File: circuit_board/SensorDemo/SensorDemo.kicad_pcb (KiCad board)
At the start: 2 copper layers, 14 parts, among them J1 BARREL_JACK, SW1 SWITCH_SPDT, U1 TLV1117-33CDCYR, U2 MCP4821, U3 dsPIC33EP32GP502

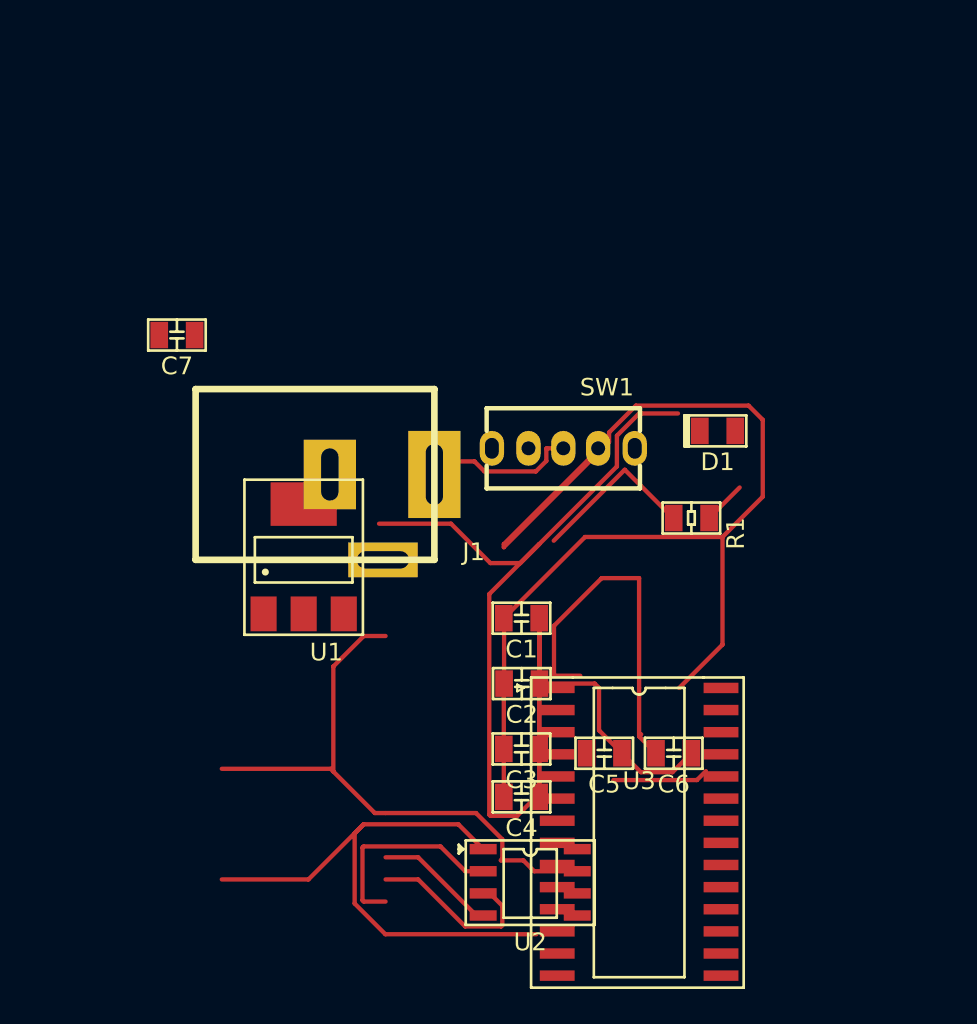
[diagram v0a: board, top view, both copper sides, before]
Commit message: updated schematic
added footprints to everything and minor changes to 6pin
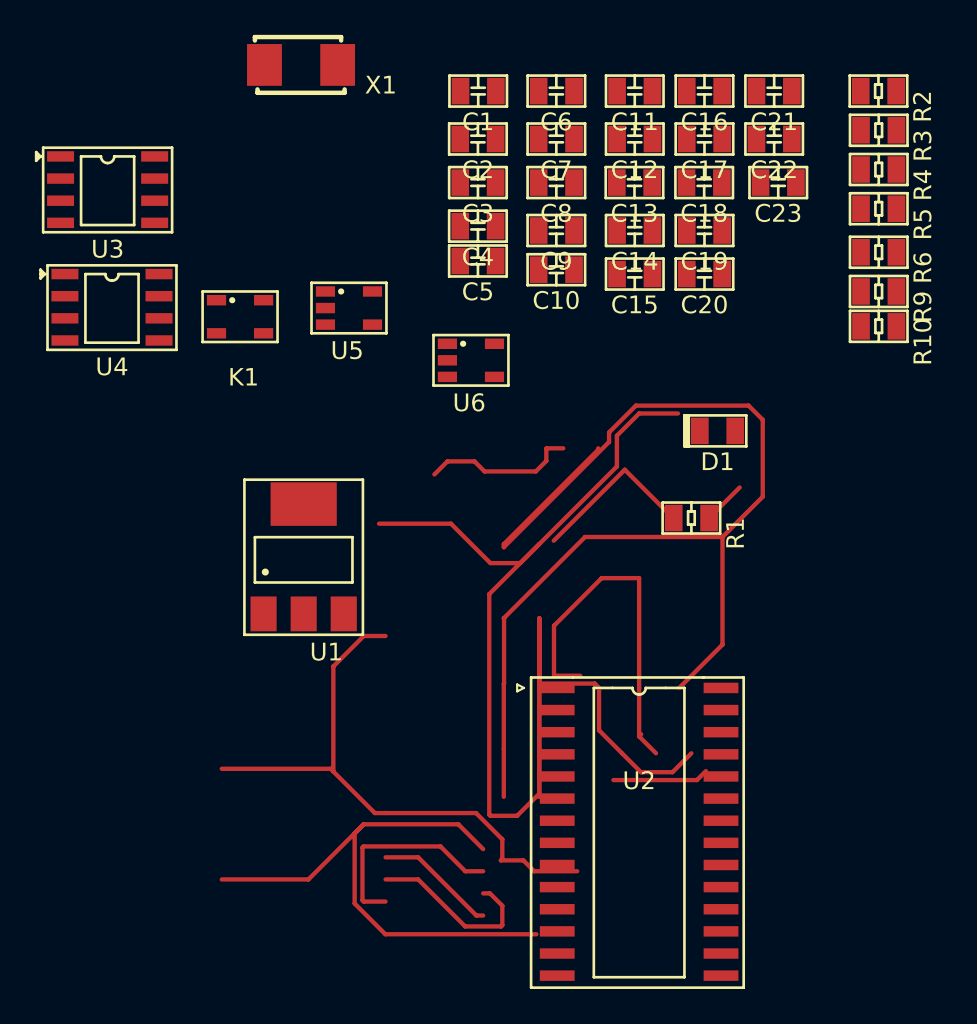
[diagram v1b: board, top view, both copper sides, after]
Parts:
- removed J1: BARREL_JACK, Global PCB Library:BARREL_JACK
- removed SW1: SWITCH_SPDT, SensorDemo_pcb:SW_OS102011MA1QN1
- removed the U2 at (88.0, 80.5)
- added C10: 0.1uF, SensorDemo_pcb:C0805, F.Cu at (89.5, 47.2)
- added C11: 0.1uF, SensorDemo_pcb:C0805, F.Cu at (94.0, 37.0)
- added C12: 1uF, SensorDemo_pcb:C0805, F.Cu at (94.0, 39.8)
- added C13: .1uF, SensorDemo_pcb:C0805, F.Cu at (94.0, 42.2)
- added C14: 0.1uF, SensorDemo_pcb:C0805, F.Cu at (94.0, 45.0)
- added C15: 1uF, SensorDemo_pcb:C0805, F.Cu at (94.0, 47.5)
- added C16: 0.1uF, SensorDemo_pcb:C0805, F.Cu at (98.0, 37.0)
- added C17: 1uF, SensorDemo_pcb:C0805, F.Cu at (98.0, 39.8)
- added C18: .1uF, SensorDemo_pcb:C0805, F.Cu at (98.0, 42.2)
- added C19: 0.1uF, SensorDemo_pcb:C0805, F.Cu at (98.0, 45.0)
- added C20: 1uF, SensorDemo_pcb:C0805, F.Cu at (98.0, 47.5)
- added C21: 1uF, SensorDemo_pcb:C0805, F.Cu at (102.0, 37.0)
- added C22: .1uF, SensorDemo_pcb:C0805, F.Cu at (102.0, 39.8)
- added C23: .1uF, SensorDemo_pcb:C0805, F.Cu at (102.2, 42.2)
- added C8: 0.1uF, SensorDemo_pcb:C0805, F.Cu at (89.5, 42.2)
- added C9: 1uF, SensorDemo_pcb:C0805, F.Cu at (89.5, 45.0)
- added K1: PB, SensorDemo_pcb:SOT-23-4, F.Cu at (70.0, 49.0)
- added R10: 0, SensorDemo_pcb:R0805, F.Cu at (108.0, 50.5)
- added R2: R, SensorDemo_pcb:R0805, F.Cu at (108.0, 37.0)
- added R3: 10k, SensorDemo_pcb:R0805, F.Cu at (108.0, 39.2)
- added R4: R, SensorDemo_pcb:R0805, F.Cu at (108.0, 41.5)
- added R5: 0, SensorDemo_pcb:R0805, F.Cu at (108.0, 43.8)
- added R6: 100R, SensorDemo_pcb:R0805, F.Cu at (108.0, 46.2)
- added R9: 100R, SensorDemo_pcb:R0805, F.Cu at (108.0, 48.5)
- added U3: LTC1658, SensorDemo_pcb:SOIC-8, F.Cu at (63.8, 40.8)
- added U4: INA126, SensorDemo_pcb:SOIC-8, F.Cu at (64.0, 47.5)
- added U5: REF1925, SensorDemo_pcb:SOT-23-5, F.Cu at (76.2, 48.5)
- added U6: REF1925, SensorDemo_pcb:SOT-23-5, F.Cu at (83.2, 51.5)
- added X1: CRYSTAL, SensorDemo_pcb:CRYSTAL_ABM3-8.000MHz-D2Y-T, F.Cu at (74.8, 35.5)
- C1: value 10uF -> C
- C2: value 1uF -> .01uF
- C3: value 1uF -> C
- C4: value 100nF -> 0.1uF
- C5: value 100nF -> 10nF
- C6: value 1uF -> 10uF
- C7: value 100nF -> 1uF
- R1: value 330R -> 1k
- moved C6 38.6 mm to (89.5, 37.0)
- moved C4 32.8 mm to (85.0, 44.8)
- moved C3 32.6 mm to (85.0, 42.2)
- moved C2 31.4 mm to (85.0, 39.8)
- moved C1 30.4 mm to (85.0, 37.0)
- moved C5 29.2 mm to (85.0, 46.8)
- moved C7 24.5 mm to (89.5, 39.8)
- renumbered U3 to U2
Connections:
- C1 pad 2: Net-(C1-Pad2) -> GND
- C2 pad 1: Net-(C1-Pad1) -> Net-(C2-Pad1)
- C2 pad 2: Net-(C1-Pad2) -> GND
- C3 pad 1: Net-(C1-Pad1) -> Net-(C3-Pad1)
- C3 pad 2: Net-(C1-Pad2) -> GND
- C4 pad 1: Net-(C1-Pad1) -> /Vref
- C4 pad 2: Net-(C1-Pad2) -> GND
- C5 pad 1: Net-(C1-Pad1) -> Net-(C10-Pad1)
- C5 pad 2: Net-(C1-Pad2) -> GND
- C6 pad 1: +3V3 -> Net-(C10-Pad1)
- C6 pad 2: Net-(C1-Pad2) -> GND
- C7 pad 1: +3V3 -> Net-(C10-Pad1)
- C7 pad 2: Net-(C1-Pad2) -> GND
- D1 pad 2: Net-(C1-Pad2) -> GND
- U1 pad 1: Net-(C1-Pad2) -> GND
- U1 pad 3: Net-(C1-Pad1) -> Net-(C10-Pad1)
- U2 pad 1: (no net) -> Net-(C2-Pad1)
- U2 pad 10: (no net) -> Net-(U2-Pad10)
- U2 pad 11: (no net) -> Net-(U2-Pad11)
- U2 pad 12: (no net) -> Net-(U2-Pad12)
- U2 pad 14: (no net) -> Net-(U2-Pad14)
- U2 pad 15: /~CS -> Net-(U2-Pad15)
- U2 pad 16: /SCK -> Net-(U2-Pad16)
- U2 pad 17: /SDI -> Net-(U2-Pad17)
- U2 pad 18: (no net) -> Net-(U2-Pad18)
- U2 pad 2: (no net) -> /sensVal
- U2 pad 20: (no net) -> Net-(TC1-Pad1)
- U2 pad 21: (no net) -> /ucTX
- U2 pad 22: (no net) -> /ucRX
- U2 pad 23: (no net) -> Net-(U2-Pad23)
- U2 pad 24: (no net) -> Net-(U2-Pad24)
- U2 pad 25: (no net) -> Net-(U2-Pad25)
- U2 pad 26: (no net) -> Net-(U2-Pad26)
- U2 pad 28: (no net) -> Net-(C8-Pad1)
- U2 pad 3: (no net) -> Net-(U2-Pad3)
- U2 pad 4: (no net) -> GND
- U2 pad 5: (no net) -> /Vref
- U2 pad 6: (no net) -> /PGC
- U2 pad 7: (no net) -> /PGD
- U2 pad 9: (no net) -> Net-(U2-Pad9)

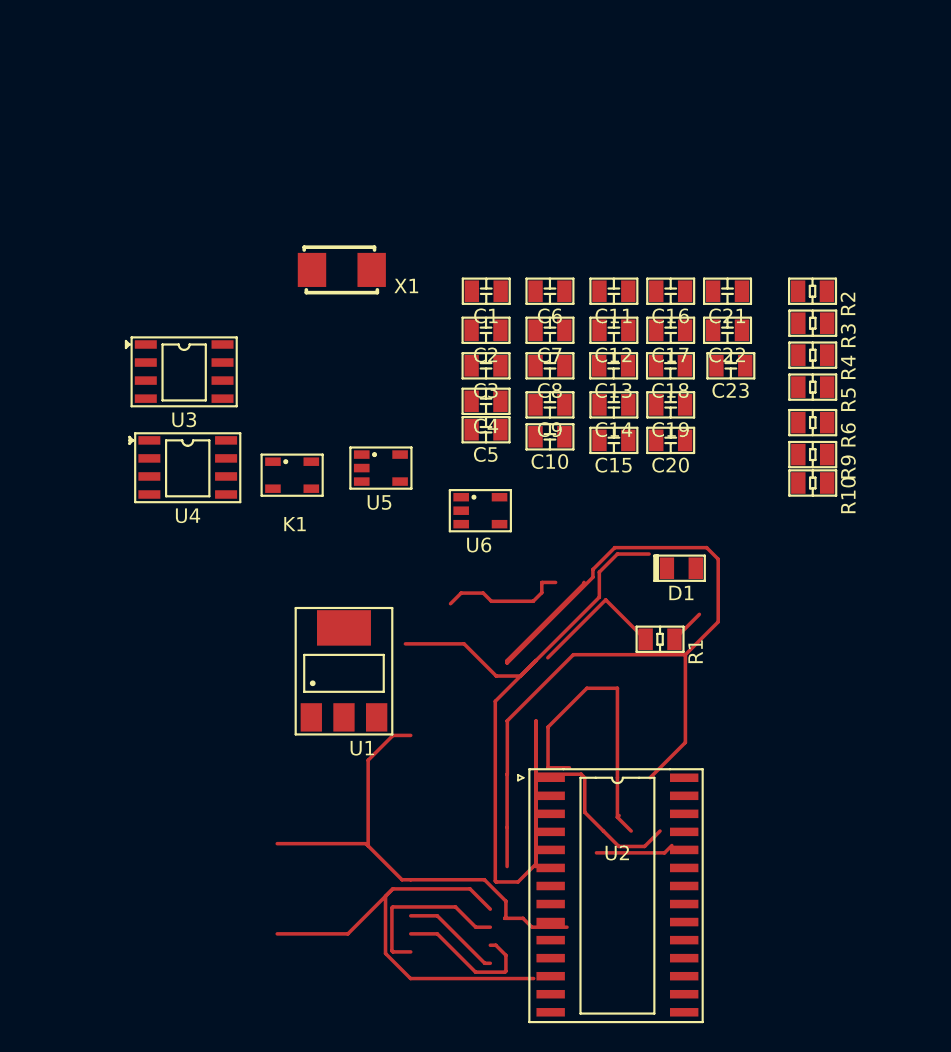
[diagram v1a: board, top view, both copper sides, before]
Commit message: update schematic
pcb parts in place. need to connect traces
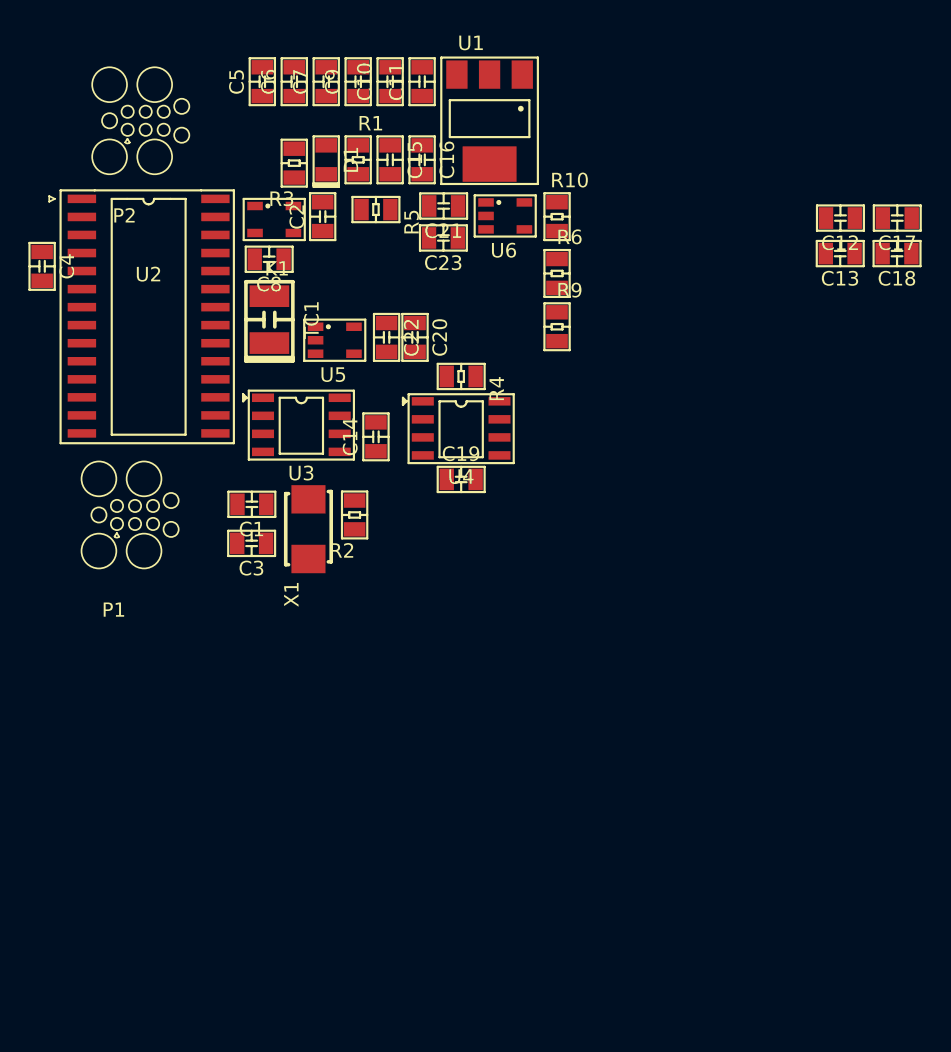
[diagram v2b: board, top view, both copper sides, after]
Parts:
- added P1: CONN3X2, SensorDemo_pcb:TC2030, F.Cu at (57.8, 52.8)
- added P2: CONN3X2, SensorDemo_pcb:TC2030, F.Cu at (58.5, 25.0)
- added TC1: 10uF, SensorDemo_pcb:C1210, F.Cu at (69.8, 39.0)
- moved U2 52.4 mm to (61.2, 30.5)
- moved U1 46.4 mm to (85.2, 21.8), turned to 180 degrees
- moved R1 39.9 mm to (76.0, 27.8), turned to 90 degrees
- moved R3 38.2 mm to (71.5, 28.0), turned to 270 degrees
- moved D1 38.1 mm to (73.8, 27.8), turned to 90 degrees
- moved R2 35.9 mm to (75.8, 52.8), turned to 270 degrees
- moved R5 33.2 mm to (77.2, 31.2)
- moved C4 32.7 mm to (53.8, 35.2), turned to 90 degrees
- moved C5 29.1 mm to (69.2, 22.2), turned to 270 degrees
- moved C10 27.4 mm to (78.2, 22.2), turned to 270 degrees
- moved C9 26.5 mm to (76.0, 22.2), turned to 270 degrees
- moved R10 26.0 mm to (90.0, 31.8), turned to 90 degrees
- moved C15 25.3 mm to (78.2, 27.8), turned to 90 degrees
- moved R4 24.8 mm to (83.2, 43.0)
- moved C22 24.0 mm to (78.0, 40.2), turned to 90 degrees
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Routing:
- net Net-(C1-Pad2): track 75.8 -> 0.00 mm
- net +3V3: track 69.1 -> 0.00 mm
- net Net-(C1-Pad1): track 68.9 -> 0.00 mm
- net GND: track 33.4 -> 0.00 mm
- net /~CS: track 11.9 -> 0.00 mm
- net /SCK: track 10.4 -> 0.00 mm
- net Net-(J1-Pad1): track 8.91 -> 0.00 mm
- net /SDI: track 6.98 -> 0.00 mm
- net Net-(D1-Pad1): track 2.48 -> 0.00 mm

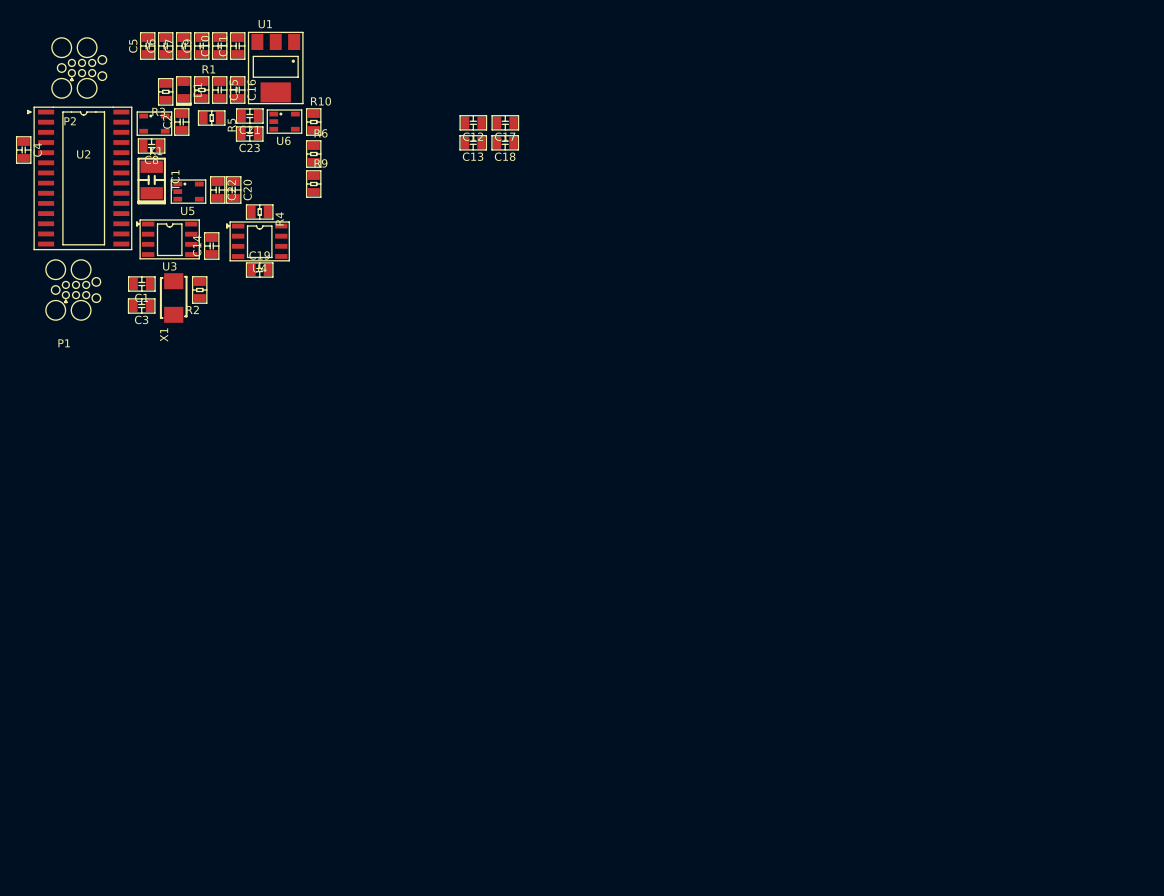
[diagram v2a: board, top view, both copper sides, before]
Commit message: updated schematic
-spaced parts
-filled ground layer
-added vias
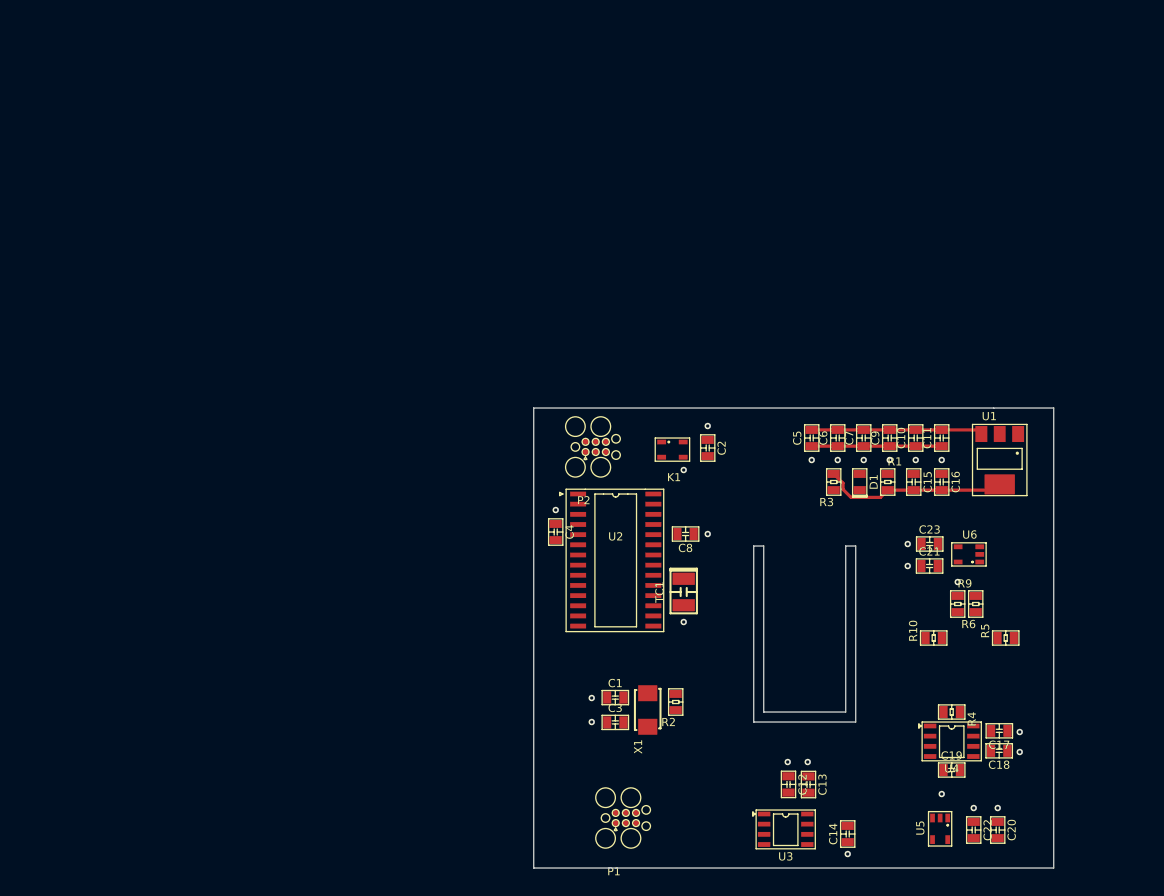
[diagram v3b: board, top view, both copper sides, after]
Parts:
- moved U5 124.7 mm to (169.2, 118.8), turned to 270 degrees
- moved C20 124.6 mm to (175.5, 120.2)
- moved C22 123.8 mm to (172.5, 120.2)
- moved R5 118.6 mm to (176.5, 96.2), turned to 180 degrees
- moved C14 108.3 mm to (156.8, 120.8)
- moved C19 106.7 mm to (169.8, 112.8)
- moved R4 106.7 mm to (169.8, 105.5)
- moved U4 106.7 mm to (169.8, 107.2)
- moved U3 106.6 mm to (149.0, 118.2)
- moved U6 104.5 mm to (173.2, 86.8), turned to 180 degrees
- moved U1 102.9 mm to (175.8, 70.8)
- moved C21 101.9 mm to (167.0, 87.2), turned to 180 degrees
- moved R10 100.8 mm to (167.5, 96.2), turned to 180 degrees
- moved C11 100.7 mm to (168.5, 71.2)
- moved C16 100.7 mm to (168.5, 76.8)
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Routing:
- net +3V3: track 0.00 -> 23.3 mm
- net Net-(C10-Pad1): track 0.00 -> 21.4 mm
- net GND: track 0.00 -> 16.2 mm
- net (no net): vias 0 -> 24
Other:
- board outline added: 65 x 57.5 mm
